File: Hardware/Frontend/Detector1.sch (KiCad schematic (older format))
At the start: 27 parts, among them J1 Conn_Coaxial, U1 OPA145ID, U2 OPA145ID, U3 OPA145ID

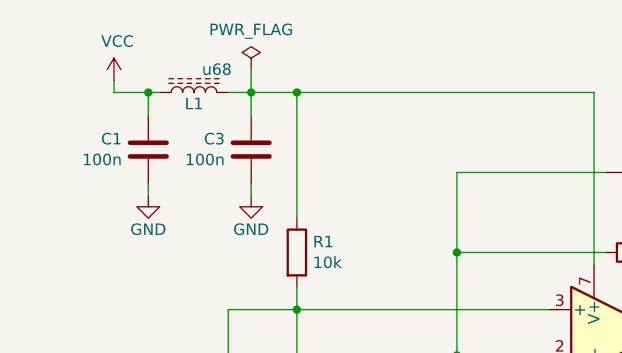
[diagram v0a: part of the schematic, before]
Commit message: add bom
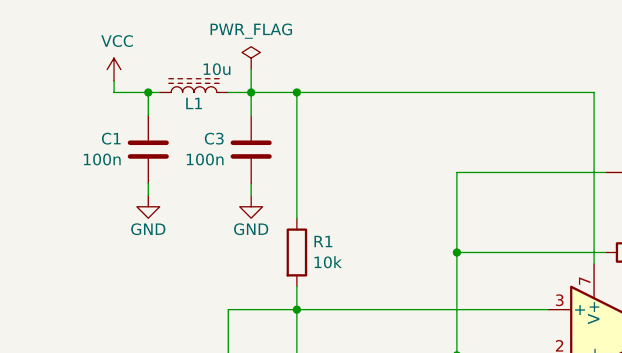
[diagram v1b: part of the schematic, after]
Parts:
- L1: value u68 -> 10u
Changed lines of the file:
@@
 AR Path="/6126BC2D/61297D41" Ref="L1"  Part="1"
 F 0 "L1" V 2550 2600 50  0000 C CNN
-F 1 "u68" V 2700 2700 50  0000 C CNN
+F 1 "10u" V 2700 2700 50  0000 C CNN
 F 2 "Inductor_SMD:L_0805_2012Metric" H 2600 2600 50  0001 C CNN
 F 3 "" H 2600 2600 50  0001 C CNN
